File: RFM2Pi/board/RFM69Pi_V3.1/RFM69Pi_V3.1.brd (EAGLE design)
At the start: 27.9 x 32.4 mm, 18 parts, among them IC1 ATMEGA168

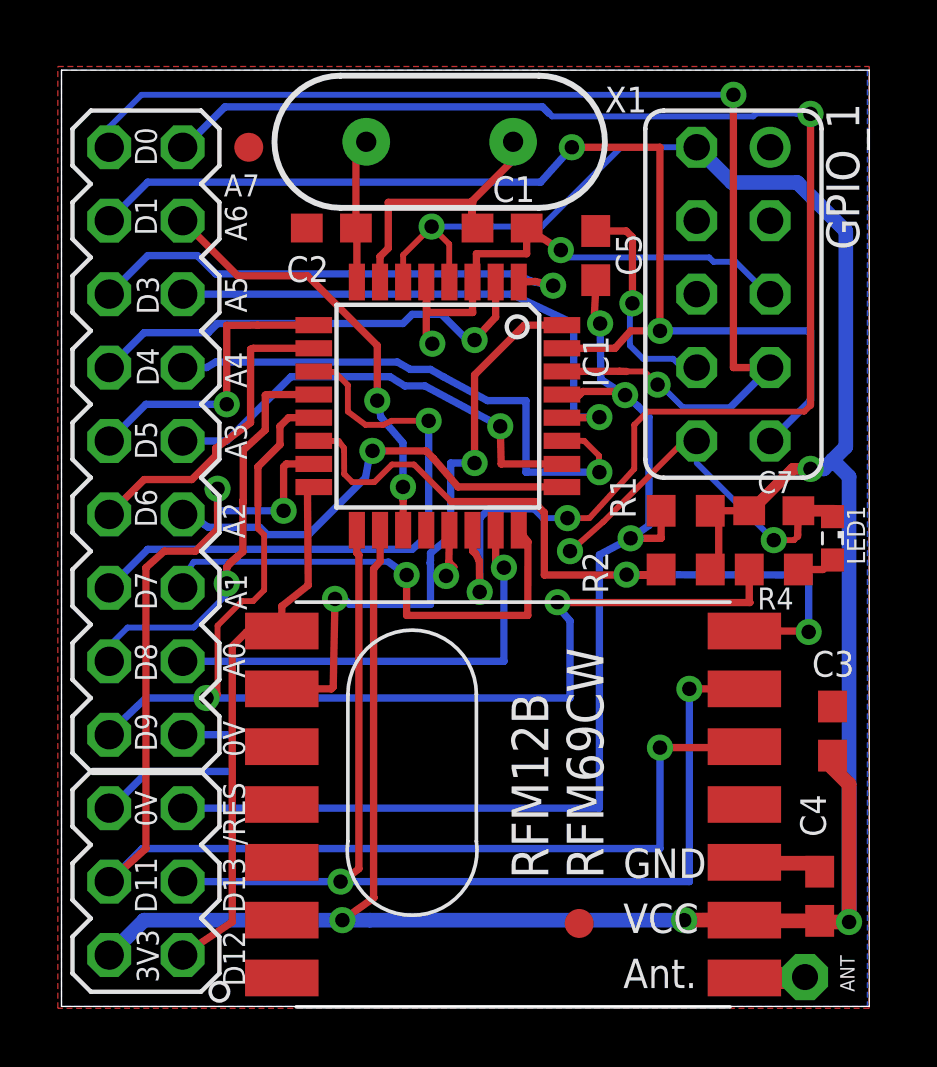
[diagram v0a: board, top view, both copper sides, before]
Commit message: add RFM12Pi V3.1
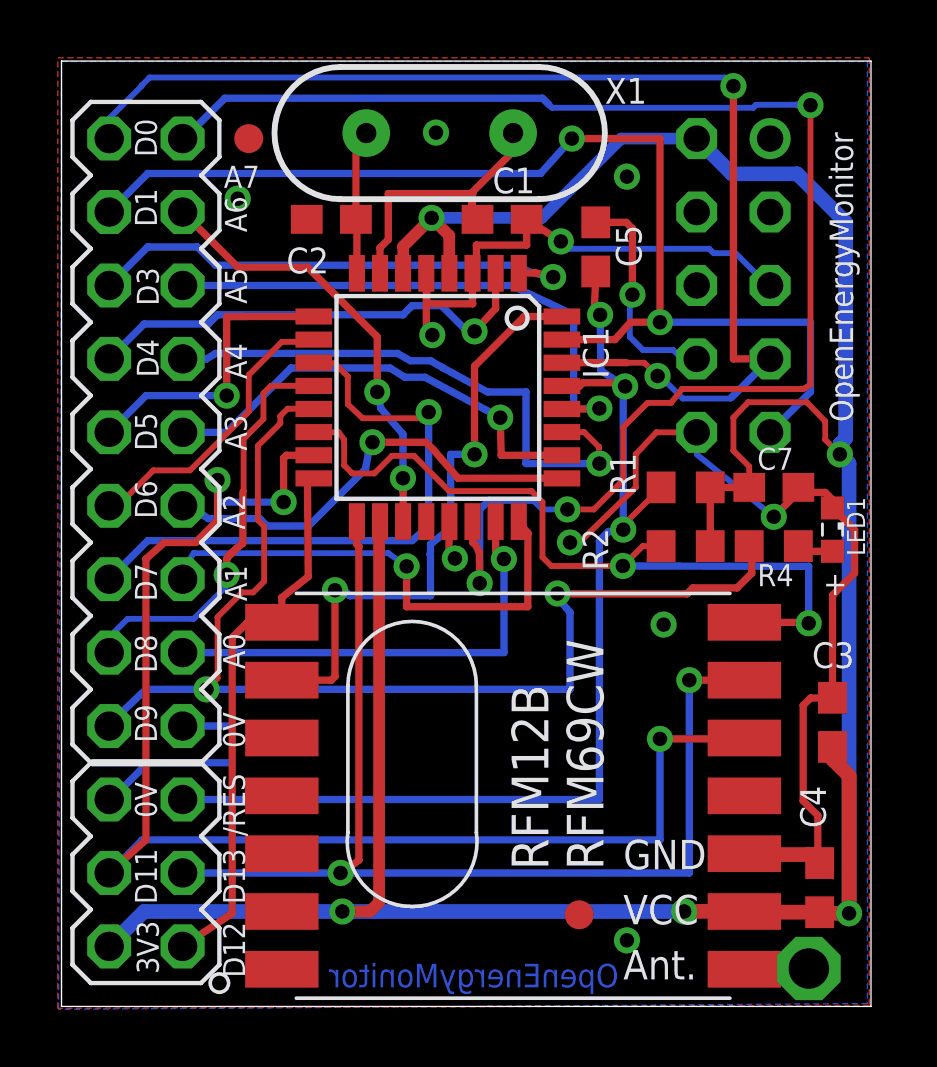
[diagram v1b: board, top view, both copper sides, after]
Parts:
- removed ANT: (no value), JeeLabs:1,6/0,8
- added ANT1: (no value), discrete:PAD-01
- R4: value 220R -> 1K
- moved C7 0.81 mm to (24.6, 18.0)
- moved R1 0.81 mm to (21.6, 18.0)
- moved R2 0.81 mm to (21.6, 15.9)
- moved R4 0.81 mm to (24.6, 15.9)
- moved C1 0.30 mm to (15.2, 27.2)
- moved C2 0.30 mm to (9.33, 27.2)
- moved C5 0.30 mm to (18.5, 26.3)
- moved LED1 0.30 mm to (26.7, 16.5)
- moved U$2 0.30 mm to (6.48, 30.0)
- moved X1 0.30 mm to (13.1, 30.2)
- moved C4 0.30 mm to (26.2, 4.11)
- moved RFM12B-RFM69CW 0.30 mm to (15.6, 7.29)
- moved U$1 0.30 mm to (17.9, 3.17)
- moved C3 0.30 mm to (26.7, 9.82)
- moved PL2 0.30 mm to (2.92, 16.0)
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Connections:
- net N$6: now also ANT1.1; no longer ANT.1
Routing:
- net GND: track 46.0 -> 60.2 mm, vias 5 -> 10
- net +3V3: track 100.6 -> 104.0 mm
- net N$6: track 2.11 -> 4.30 mm
- net D10: track 28.9 -> 27.3 mm
- net RESET: track 39.1 -> 38.3 mm
- net D6: track 11.0 -> 10.2 mm
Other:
- board size 27.9 x 32.4 mm -> 28 x 32.7 mm
- board text added: "+"
- board text added: "433Mhz 165mm Ant"
- board text added: "868Mhz 82mm Ant"
- board text added: "OpenEnergyMonitor"
- board text added: "RFM69Pi V3.1 January 15 RaspberryPi RF Expansion OpenEnergyMonitor.org"
- board text removed: "RFM69Pi V3 Nov14 RaspberryPi RF Expansion OpenEnergyMonitor.org"
